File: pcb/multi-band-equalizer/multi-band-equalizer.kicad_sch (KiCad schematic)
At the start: 154 parts, among them J1 TagConnect_TC2030, J2 Output Audio, J3 Barrel_Jack_Switch, J4 Input Audio, J5 Conn_01x06_Socket, Q1 SI2347DS-T1-BE3, SW1 SW_Push, U1 CS4272, U2 STM32H7B0VBT6, U3 SPX3819M5-L-3-3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

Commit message: new gerbers
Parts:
- C10, C4, C5, C6, C7, C8, C9: value 100n -> 1u
- C3: value 2u2 -> 10u
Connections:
- net ASIGNAL_IN_L: now also J5.1 (Pin_1); no longer J5.6 (Pin_6)
- net ASIGNAL_IN_R: now also J5.2 (Pin_2); no longer J5.5 (Pin_5)
- net ASIGNAL_OUT_L: now also J5.3 (Pin_3); no longer J5.4 (Pin_4)
- net ASIGNAL_OUT_R: now also J5.4 (Pin_4); no longer J5.3 (Pin_3)
- net CODEC_AOUT_L: now also J5.6 (Pin_6); no longer J5.1 (Pin_1)
- net CODEC_AOUT_R: now also J5.5 (Pin_5); no longer J5.2 (Pin_2)
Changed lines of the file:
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@@
 	(wire
 		(pts
-			(xy 473.71 434.34) (xy 490.22 434.34)
-		)
-		(stroke
-			(width 0)
-			(type default)
-		)
-	)
-	(wire
-		(pts
 			(xy 632.46 485.14) (xy 632.46 494.03)
 		)
@@
 	(wire
 		(pts
-			(xy 345.44 389.89) (xy 326.39 389.89)
+			(xy 473.71 431.8) (xy 490.22 431.8)
 		)
 		(stroke
@@
 	(wire
 		(pts
-			(xy 377.19 422.91) (xy 392.43 422.91)
+			(xy 345.44 389.89) (xy 326.39 389.89)
 		)
 		(stroke
@@
 	(wire
 		(pts
-			(xy 367.03 481.33) (xy 386.08 481.33)
+			(xy 377.19 422.91) (xy 392.43 422.91)
 		)
 		(stroke
@@
 	(wire
 		(pts
-			(xy 472.44 100.33) (xy 516.89 100.33)
+			(xy 367.03 481.33) (xy 386.08 481.33)
 		)
 		(stroke
@@
 	(wire
 		(pts
-			(xy 585.47 472.44) (xy 585.47 477.52)
+			(xy 472.44 100.33) (xy 516.89 100.33)
 		)
 		(stroke
@@
 	(wire
 		(pts
-			(xy 459.74 214.63) (xy 464.82 214.63)
+			(xy 585.47 472.44) (xy 585.47 477.52)
 		)
 		(stroke
@@
 	(wire
 		(pts
-			(xy 622.3 438.15) (xy 622.3 439.42)
+			(xy 459.74 214.63) (xy 464.82 214.63)
 		)
 		(stroke
@@
 	(wire
 		(pts
-			(xy 535.94 180.34) (xy 535.94 200.66)
+			(xy 622.3 438.15) (xy 622.3 439.42)
 		)
 		(stroke
@@
 	(wire
 		(pts
-			(xy 473.71 439.42) (xy 490.22 439.42)
+			(xy 535.94 180.34) (xy 535.94 200.66)
 		)
 		(stroke
@@
 	(wire
 		(pts
+			(xy 473.71 434.34) (xy 490.22 434.34)
+		)
+		(stroke
+			(width 0)
+			(type default)
+		)
+	)
+	(wire
+		(pts
 			(xy 474.98 280.67) (xy 474.98 283.21)
 		)
@@
 	(wire
 		(pts
+			(xy 473.71 436.88) (xy 490.22 436.88)
+		)
+		(stroke
+			(width 0)
+			(type default)
+		)
+	)
+	(wire
+		(pts
 			(xy 480.06 481.33) (xy 480.06 485.14)
 		)
@@
 	(wire
 		(pts
-			(xy 473.71 436.88) (xy 490.22 436.88)
-		)
-		(stroke
-			(width 0)
-			(type default)
-		)
-	)
-	(wire
-		(pts
 			(xy 444.5 93.98) (xy 457.2 93.98)
 		)
@@
 	(wire
 		(pts
-			(xy 162.56 494.03) (xy 179.07 494.03)
+			(xy 473.71 441.96) (xy 490.22 441.96)
 		)
 		(stroke
@@
 	(wire
 		(pts
-			(xy 176.53 401.32) (xy 186.69 401.32)
+			(xy 162.56 494.03) (xy 179.07 494.03)
 		)
 		(stroke
@@
 	(wire
 		(pts
-			(xy 622.3 421.64) (xy 622.3 420.37)
+			(xy 176.53 401.32) (xy 186.69 401.32)
 		)
 		(stroke
@@
 	(wire
 		(pts
-			(xy 351.79 271.78) (xy 351.79 269.24)
+			(xy 622.3 421.64) (xy 622.3 420.37)
 		)
 		(stroke
@@
 	(wire
 		(pts
-			(xy 454.66 182.88) (xy 454.66 180.34)
+			(xy 351.79 271.78) (xy 351.79 269.24)
 		)
 		(stroke
@@
 	(wire
 		(pts
-			(xy 473.71 441.96) (xy 490.22 441.96)
+			(xy 454.66 182.88) (xy 454.66 180.34)
 		)
 		(stroke
@@
 	(wire
 		(pts
-			(xy 473.71 431.8) (xy 490.22 431.8)
-		)
-		(stroke
-			(width 0)
-			(type default)
-		)
-	)
-	(wire
-		(pts
 			(xy 290.83 289.56) (xy 311.15 289.56)
 		)
@@
 	(wire
 		(pts
-			(xy 473.71 429.26) (xy 490.22 429.26)
-		)
-		(stroke
-			(width 0)
-			(type default)
-		)
-	)
-	(wire
-		(pts
 			(xy 322.58 281.94) (xy 314.96 281.94)
 		)
@@
 	(wire
 		(pts
+			(xy 473.71 439.42) (xy 490.22 439.42)
+		)
+		(stroke
+			(width 0)
+			(type default)
+		)
+	)
+	(wire
+		(pts
 			(xy 565.15 190.5) (xy 565.15 193.04)
 		)
@@
 	(wire
 		(pts
+			(xy 473.71 429.26) (xy 490.22 429.26)
+		)
+		(stroke
+			(width 0)
+			(type default)
+		)
+	)
+	(wire
+		(pts
 			(xy 195.58 406.4) (xy 186.69 406.4)
 		)
@@
 		)
 	)
-	(label "CODEC_AOUT_R"
-		(at 473.71 431.8 0)
-		(fields_autoplaced yes)
-		(effects
-			(font
-				(size 1.27 1.27)
-			)
-			(justify left bottom)
-		)
-	)
 	(label "MCU_SWCLK"
 		(at 543.56 105.41 180)
@@
 		)
 	)
+	(label "CODEC_AOUT_L"
+		(at 473.71 441.96 0)
+		(fields_autoplaced yes)
+		(effects
+			(font
+				(size 1.27 1.27)
+			)
+			(justify left bottom)
+		)
+	)
 	(label "CTRL_KNB_30_HZ"
 		(at 586.74 260.35 180)
@@
 		)
 	)
-	(label "ASIGNAL_OUT_R"
-		(at 473.71 434.34 0)
-		(fields_autoplaced yes)
-		(effects
-			(font
-				(size 1.27 1.27)
-			)
-			(justify left bottom)
-		)
-	)
-	(label "ASIGNAL_IN_L"
-		(at 473.71 441.96 0)
+	(label "VDDA"
+		(at 501.65 224.79 0)
 		(fields_autoplaced yes)
 		(effects
@@
 		)
 	)
-	(label "VDDA"
-		(at 501.65 224.79 0)
+	(label "I2S_SCLK"
+		(at 246.38 274.32 0)
 		(fields_autoplaced yes)
 		(effects
 			(font
 				(size 1.27 1.27)
+				(thickness 0.1588)
 			)
 			(justify left bottom)
 		)
 	)
-	(label "I2S_SCLK"
-		(at 246.38 274.32 0)
+	(label "MCU_XTO"
+		(at 501.65 232.41 0)
 		(fields_autoplaced yes)
 		(effects
 			(font
 				(size 1.27 1.27)
-				(thickness 0.1588)
 			)
 			(justify left bottom)
 		)
 	)
-	(label "MCU_XTO"
-		(at 501.65 232.41 0)
+	(label "CODEC_AOUT_R"
+		(at 473.71 439.42 0)
 		(fields_autoplaced yes)
 		(effects
@@
 		)
 	)
+	(label "ASIGNAL_OUT_L"
+		(at 473.71 434.34 0)
+		(fields_autoplaced yes)
+		(effects
+			(font
+				(size 1.27 1.27)
+			)
+			(justify left bottom)
+		)
+	)
 	(label "ASIGNAL_IN_L"
 		(at 377.19 417.83 0)
@@
 		)
 	)
-	(label "ASIGNAL_IN_R"
-		(at 473.71 439.42 0)
-		(fields_autoplaced yes)
-		(effects
-			(font
-				(size 1.27 1.27)
-			)
-			(justify left bottom)
-		)
-	)
 	(label "CODEC_AOUT_R"
 		(at 514.35 394.97 180)
@@
 		)
 	)
-	(label "CODEC_AOUT_L"
+	(label "ASIGNAL_IN_L"
 		(at 473.71 429.26 0)
 		(fields_autoplaced yes)
@@
 		)
 	)
-	(label "ASIGNAL_OUT_L"
-		(at 473.71 436.88 0)
-		(fields_autoplaced yes)
-		(effects
-			(font
-				(size 1.27 1.27)
-			)
-			(justify left bottom)
-		)
-	)
 	(label "CODEC_VFILT"
 		(at 304.8 259.08 180)
@@
 		)
 	)
+	(label "ASIGNAL_OUT_R"
+		(at 473.71 436.88 0)
+		(fields_autoplaced yes)
+		(effects
+			(font
+				(size 1.27 1.27)
+			)
+			(justify left bottom)
+		)
+	)
 	(label "ASIGNAL_IN_R+"
 		(at 236.22 147.32 180)
@@
 		)
 	)
+	(label "ASIGNAL_IN_R"
+		(at 473.71 431.8 0)
+		(fields_autoplaced yes)
+		(effects
+			(font
+				(size 1.27 1.27)
+			)
+			(justify left bottom)
+		)
+	)
 	(symbol
 		(lib_id "Device:C")
@@
 			)
 		)
-		(property "Value" "100n"
+		(property "Value" "1u"
 			(at 483.87 187.9599 0)
 			(effects
@@
 			)
 		)
-		(property "Value" "100n"
+		(property "Value" "1u"
 			(at 568.96 187.9599 0)
 			(effects
@@
 			)
 		)
-		(property "Value" "2u2"
+		(property "Value" "10u"
 			(at 445.77 187.9599 0)
 			(effects
@@
 			)
 		)
-		(property "Value" "100n"
+		(property "Value" "1u"
 			(at 471.17 187.9599 0)
 			(effects
@@
 			)
 		)
-		(property "Value" "100n"
+		(property "Value" "1u"
 			(at 496.57 187.9599 0)
 			(effects
@@
 			)
 		)
-		(property "Value" "100n"
+		(property "Value" "1u"
 			(at 521.97 187.9599 0)
 			(effects
@@
 			)
 		)
-		(property "Value" "100n"
+		(property "Value" "1u"
 			(at 509.27 187.9599 0)
 			(effects
@@
 			)
 		)
-		(property "Value" "100n"
+		(property "Value" "1u"
 			(at 458.47 187.9599 0)
 			(effects

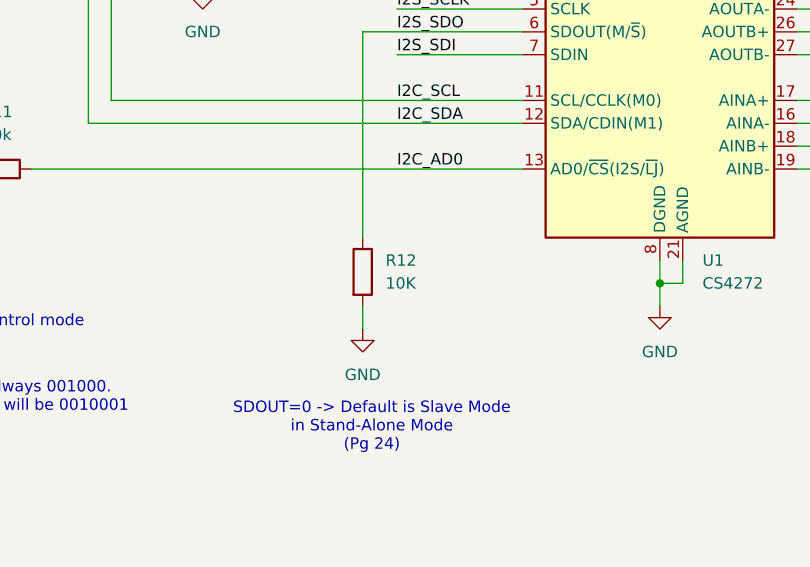
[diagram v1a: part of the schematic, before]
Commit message: resistor value
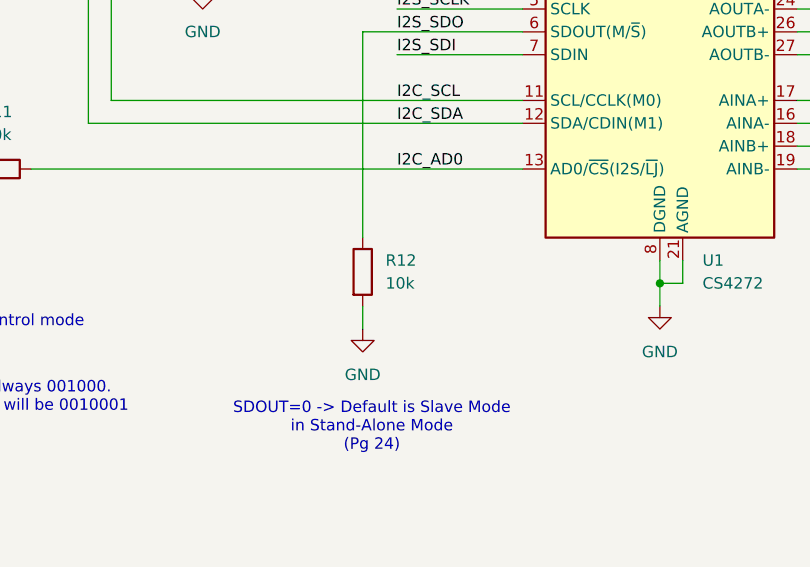
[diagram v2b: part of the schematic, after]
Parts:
- R12: value 10K -> 10k
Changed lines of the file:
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@@
 			)
 		)
-		(property "Value" "10K"
+		(property "Value" "10k"
 			(at 245.11 304.7999 0)
 			(effects
